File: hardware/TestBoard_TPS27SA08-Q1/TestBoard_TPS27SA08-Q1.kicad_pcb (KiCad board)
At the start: 2 copper layers, 59.8 x 92 mm, 99 parts, among them J1 575-4, J10 Conn_01x04, J11 Conn_01x02, J12 Conn_01x02, J14 Conn_01x02, J15 Conn_01x06, J2 575-4, J3 575-4, J4 575-4, J7 Conn_01x02, J8 Conn_01x02, J9 Conn_01x02, Q1 SQJ141ELP, U1 TPS27SA08-Q1, U2 Logic Analyzer, U3 MCP23S17-E/SO, U4 NUCLEO_L432KC

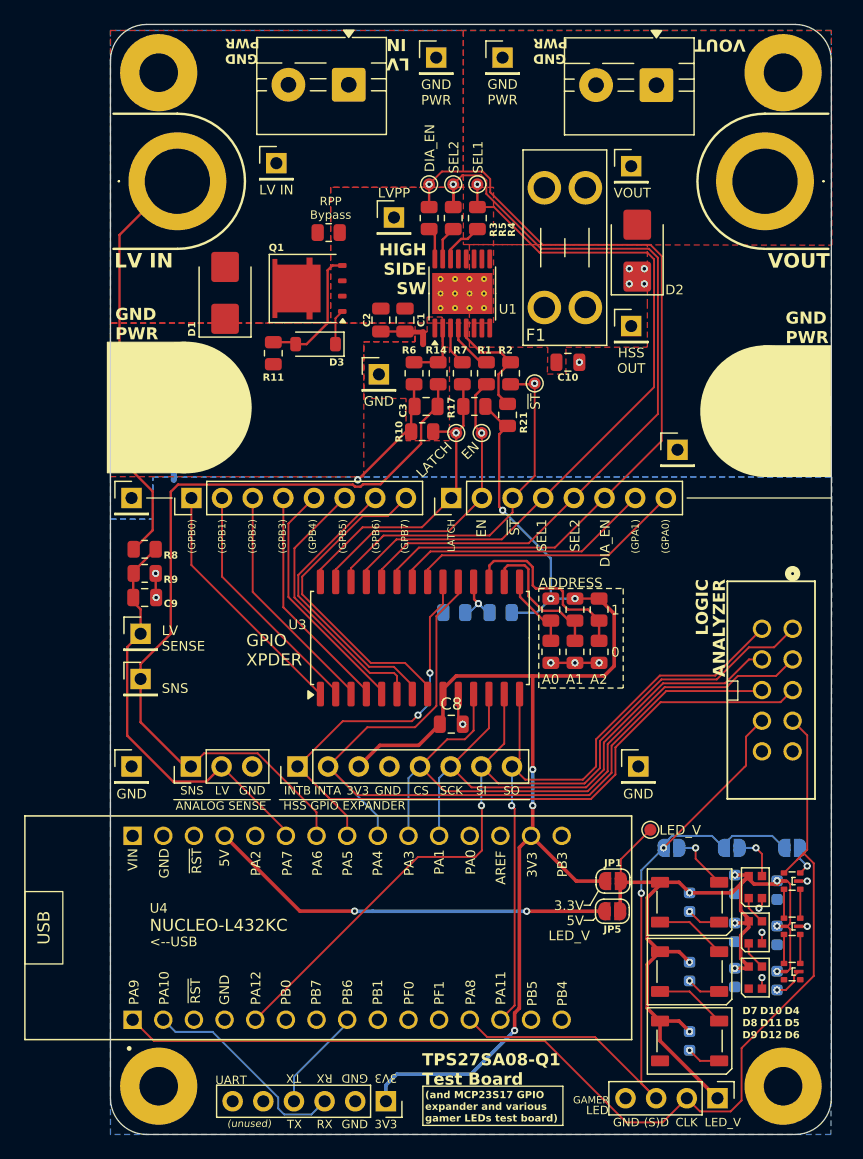
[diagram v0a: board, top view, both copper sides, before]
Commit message: revisions (dip switch for address, leds on gpio outputs, logic analyzer pinout?, ...)
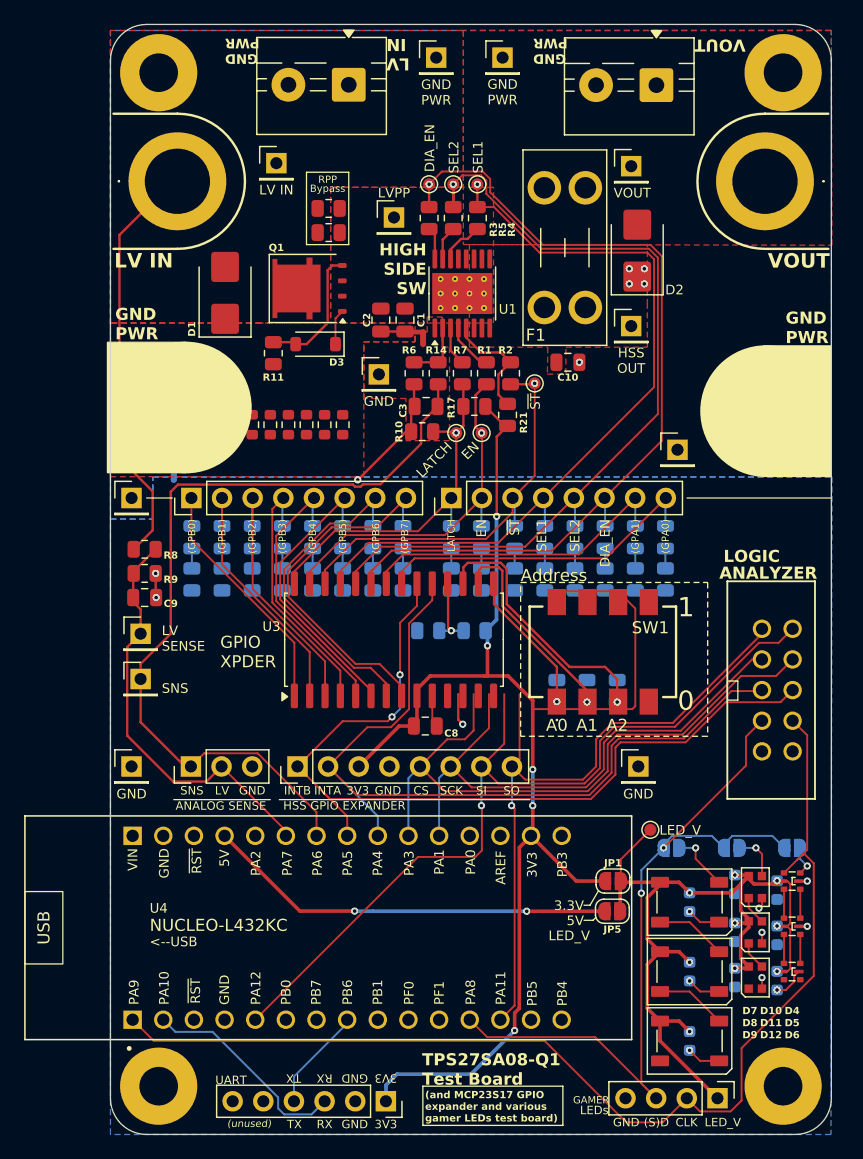
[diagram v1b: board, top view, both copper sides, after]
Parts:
- added D13: LED_Small, LED_SMD:LED_0805_2012Metric, B.Cu at (156.2, 88.2)
- added D14: LED_Small, LED_SMD:LED_0805_2012Metric, B.Cu at (153.8, 88.2)
- added D15: LED_Small, LED_SMD:LED_0805_2012Metric, B.Cu at (151.2, 88.2)
- added D16: LED_Small, LED_SMD:LED_0805_2012Metric, B.Cu at (148.8, 88.2)
- added D17: LED_Small, LED_SMD:LED_0805_2012Metric, B.Cu at (146.2, 88.2)
- added D18: LED_Small, LED_SMD:LED_0805_2012Metric, B.Cu at (143.8, 88.2)
- added D19: LED_Small, LED_SMD:LED_0805_2012Metric, B.Cu at (141.0, 88.2)
- added D20: LED_Small, LED_SMD:LED_0805_2012Metric, B.Cu at (138.5, 88.2)
- added D21: LED_Small, LED_SMD:LED_0805_2012Metric, B.Cu at (117.0, 88.2)
- added D22: LED_Small, LED_SMD:LED_0805_2012Metric, B.Cu at (119.5, 88.2)
- added D23: LED_Small, LED_SMD:LED_0805_2012Metric, B.Cu at (122.0, 88.2)
- added D24: LED_Small, LED_SMD:LED_0805_2012Metric, B.Cu at (124.5, 88.2)
- added D25: LED_Small, LED_SMD:LED_0805_2012Metric, B.Cu at (127.0, 88.2)
- added D26: LED_Small, LED_SMD:LED_0805_2012Metric, B.Cu at (129.5, 88.2)
- added D27: LED_Small, LED_SMD:LED_0805_2012Metric, B.Cu at (132.0, 88.2)
- added D28: LED_Small, LED_SMD:LED_0805_2012Metric, B.Cu at (134.5, 88.2)
- added G***: LHRs_LOGO, UTSVT_Logos:LHRs_LOGO, B.Cu at (143.2, 135.2)
- added R15: 1k, Resistor_SMD:R_0805_2012Metric, B.Cu at (156.2, 91.8)
- added R16: 1k, Resistor_SMD:R_0805_2012Metric, B.Cu at (153.8, 91.8)
- added R18: 1k, Resistor_SMD:R_0805_2012Metric, B.Cu at (151.2, 91.8)
- added R19: 1k, Resistor_SMD:R_0805_2012Metric, B.Cu at (148.8, 91.8)
- added R20: 1k, Resistor_SMD:R_0805_2012Metric, B.Cu at (146.2, 91.8)
- added R22: 1k, Resistor_SMD:R_0805_2012Metric, B.Cu at (143.8, 91.8)
- added R23: 1k, Resistor_SMD:R_0805_2012Metric, B.Cu at (141.0, 91.8)
- added R24: 1k, Resistor_SMD:R_0805_2012Metric, B.Cu at (138.5, 91.8)
- added R32: 1k, Resistor_SMD:R_0805_2012Metric, B.Cu at (124.5, 91.8)
- added R33: 1k, Resistor_SMD:R_0805_2012Metric, B.Cu at (127.0, 91.8)
- added R34: 1k, Resistor_SMD:R_0805_2012Metric, B.Cu at (129.5, 91.8)
- added R35: 1k, Resistor_SMD:R_0805_2012Metric, B.Cu at (132.0, 91.8)
- added R36: 1k, Resistor_SMD:R_0805_2012Metric, B.Cu at (134.5, 91.8)
- added R37: 0, Resistor_SMD:R_0805_2012Metric, F.Cu at (128.3, 61.0)
- added REF**: R_0603_1608Metric, Resistor_SMD:R_0603_1608Metric, F.Cu at (128.0, 78.9)
- added REF**: R_0603_1608Metric, Resistor_SMD:R_0603_1608Metric, F.Cu at (123.5, 78.9)
- added REF**: R_0603_1608Metric, Resistor_SMD:R_0603_1608Metric, F.Cu at (126.5, 78.9)
- added REF**: R_0603_1608Metric, Resistor_SMD:R_0603_1608Metric, F.Cu at (129.5, 78.9)
- added REF**: R_0603_1608Metric, Resistor_SMD:R_0603_1608Metric, F.Cu at (125.0, 78.9)
- added REF**: R_0603_1608Metric, Resistor_SMD:R_0603_1608Metric, F.Cu at (122.0, 78.9)
- added SW1: SW_DIP_x04, PowerDistributionUnitLib:ADE04S04, F.Cu at (151.1, 97.8)
- D10, D11, D12: value WS2812B -> WS2812B-2020
- R25, R26, R27, R28, R29, R30: value 0 -> 1k; moved to B.Cu
- R6: value 374 -> 392
- moved R25 33.8 mm to (117.0, 91.8), turned to -90 degrees
- moved R27 29.4 mm to (119.5, 91.8), turned to -90 degrees
- moved R29 24.9 mm to (122.0, 91.8), turned to -90 degrees
- moved R26 3.58 mm to (152.2, 101.0), turned to -90 degrees
- moved R28 3.40 mm to (149.8, 101.0), turned to -90 degrees
- moved R30 3.29 mm to (147.2, 101.0), turned to -90 degrees
- moved R13 2.63 mm to (136.6, 96.0)
- moved R31 2.63 mm to (140.4, 96.0)
- moved C8 2.16 mm to (136.3, 103.9)
- moved U3 2.16 mm to (133.8, 96.8)
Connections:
- net /DIA_EN_A renamed /GPA2
- net /EN_A renamed /GPA6
- net /LATCH_A renamed /GPA7
- net /SEL1_A renamed /GPA4
- net /SEL2_A renamed /GPA3
- net /~{ST}_A renamed /GPA5
- net Net-(J11-Pin_7) renamed /GPA1
- net Net-(J11-Pin_8) renamed /GPA0
- net Net-(J12-Pin_1) renamed /GPB0
- net Net-(J12-Pin_2) renamed /GPB1
- net Net-(J12-Pin_3) renamed /GPB2
- net Net-(J12-Pin_4) renamed /GPB3
- net Net-(J12-Pin_5) renamed /GPB4
- net Net-(J12-Pin_6) renamed /GPB5
- net Net-(J12-Pin_7) renamed /GPB6
- net Net-(J12-Pin_8) renamed /GPB7
- R25 pad 1: Net-(U3-A2) -> Net-(D21-K)
- R25 pad 2: +3V3 -> GND
- R27 pad 1: Net-(U3-A1) -> Net-(D22-K)
- R27 pad 2: +3V3 -> GND
- R29 pad 1: Net-(U3-A0) -> Net-(D23-K)
- R29 pad 2: +3V3 -> GND
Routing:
- net +3V3: track 110.5 -> 117.6 mm, vias 6 -> 5
- net Net-(U3-A1): track 12.2 -> 18.3 mm, vias 0 -> 1
- net Net-(U3-A2): track 16.2 -> 22.2 mm, vias 0 -> 1
- net Net-(U3-A0): track 5.99 -> 11.6 mm, vias 0 -> 1
- net /GPA5: track 30.3 -> 34.9 mm
- net /GPA4: track 60.0 -> 64.6 mm
- net /GPA3: track 66.2 -> 70.8 mm
- net /GPA2: track 67.9 -> 72.4 mm
- net /GPA6: track 25.6 -> 30.2 mm
- net /GPA0: track 24.2 -> 28.7 mm
- net /GPA1: track 21.9 -> 26.5 mm
- net /GPA7: track 25.8 -> 30.4 mm
- net GND: track 34.4 -> 30.4 mm, vias 16 -> 12
- net /GPB6: track 24.0 -> 27.2 mm
- net /GPB7: track 27.0 -> 30.1 mm
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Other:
- board text added: "2"
- board text added: "3"
- board text added: "4"
- board text added: "5"
- board text added: "6"
- board text added: "7"
- board text added: "Address"
- board text added: "Bypass"
- board text added: "GPIO A"
- board text added: "GPIO B"
- board text added: "LEDs"
- board text added: "RPP"
- board text added: "Rev A"
- board text removed: "ADDRESS"
- board text removed: "LED"
- board text removed: "RPP Bypass"
- board text removed: "v1.0.0"

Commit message: logic analyzer fix and other little things
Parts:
- removed REF** (x6): R_0603_1608Metric, Resistor_SMD:R_0603_1608Metric
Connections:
- U2 pad 1: /SI -> GND
- U2 pad 10: GND -> /LED_D
- U2 pad 2: /SO -> GND
- U2 pad 3: /HSS_CS -> /SI
- U2 pad 4: /SCK -> /SO
- U2 pad 5: /INTB -> /HSS_CS
- U2 pad 6: /INTA -> /SCK
- U2 pad 7: /LED_CK -> /INTB
- U2 pad 8: /LED_D -> /INTA
- U2 pad 9: GND -> /LED_CK
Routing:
- net +3V3: track 117.6 -> 135.8 mm
- net GND: track 30.4 -> 35.7 mm
- net /SCK: track 48.3 -> 43.6 mm, vias 1 -> 0
- net /HSS_CS: track 52.7 -> 49.8 mm
- net /LED_CK: track 93.7 -> 91.1 mm
- net /LED_D: track 66.1 -> 63.6 mm
- net /GPB0: track 19.9 -> 22.3 mm
- net /SI: track 71.4 -> 69.5 mm
- net /SO: track 55.8 -> 54.7 mm
- net /INTB: track 72.9 -> 71.9 mm
- net /INTA: track 69.2 -> 68.1 mm

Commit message: last revisions, export gerbers and pdf schematic
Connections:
- J9 pad 1: /INTB -> /INTA
- J9 pad 2: /INTA -> /INTB
- U2 pad 7: /INTB -> /INTA
- U2 pad 8: /INTA -> /INTB
- U3 pad 19: /INTA -> /INTB
- U3 pad 20: /INTB -> /INTA
- U4 pad CN4_8: /INTB -> /INTA
- U4 pad CN4_9: /INTA -> /INTB
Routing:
- net /INTB: track 71.9 -> 68.1 mm, vias 2 -> 0
- net /INTA: track 68.1 -> 71.9 mm, vias 0 -> 2
